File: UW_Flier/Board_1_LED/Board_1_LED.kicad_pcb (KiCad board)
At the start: 2 copper layers, 7.2 x 9.2 mm, 14 parts, among them J1 RESET, J2 SWDIO, J3 SWDCLK, J4 GND, J5 VDD, J6 LED_DRAIN, Q1 CSD13385F5, U1 EYSHSNZWZ_module_stub, Y1 Crystal

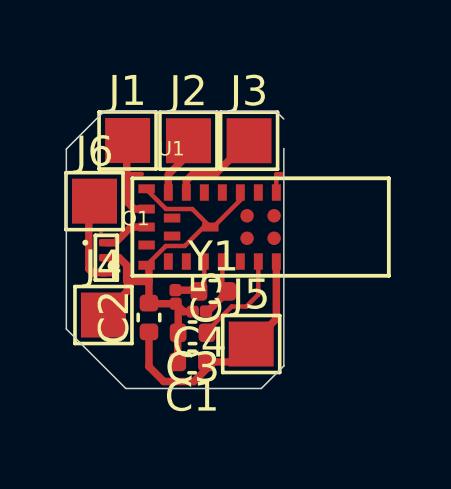
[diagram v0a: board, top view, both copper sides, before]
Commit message: added bmp384
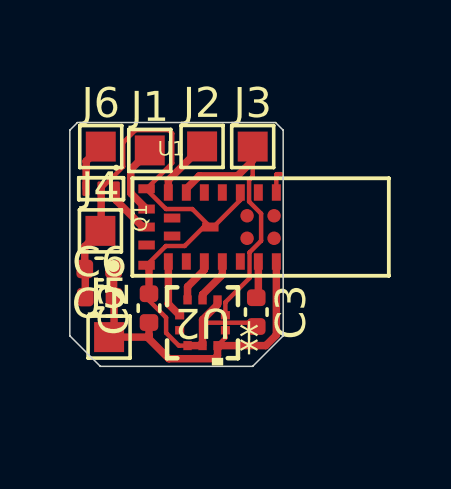
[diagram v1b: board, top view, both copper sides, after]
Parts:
- removed C4, C5: C, Capacitor_SMD:C_0201_0603Metric_Pad0.64x0.40mm_HandSolder
- removed Y1: Crystal, Capacitor_SMD:C_0402_1005Metric
- added C6: 100nF, Capacitor_SMD:C_0402_1005Metric, F.Cu at (103.6, 76.7)
- added U2: BMP384, footprints:LGA10_2.0X2.0X0.95_BOS, F.Cu at (107.0, 77.5)
- J1, J2, J3, J4, J5, J6: footprint CSD13385F5:TestPoint_Pad_1.5x1.5mm_2 -> TestPoint:TestPoint_Pad_1.0x1.0mm
- moved J5 4.74 mm to (103.9, 78.0)
- moved C1 4.38 mm to (103.6, 75.8)
- moved J4 2.81 mm to (103.6, 74.5)
- moved Q1 2.31 mm to (103.7, 73.1), turned to -90 degrees
- moved C3 2.23 mm to (108.8, 77.2), turned to -90 degrees
- moved J6 1.83 mm to (103.6, 71.7)
- moved J1 0.81 mm to (105.3, 71.8)
- moved J2 0.49 mm to (107.0, 71.7)
- moved C2 0.31 mm to (105.3, 77.1)
- moved J3 0.23 mm to (108.7, 71.7)
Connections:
- U1 pad 2: unconnected-(U1-P0.06-Pad2) -> Net-(U1-P0.06)
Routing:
- net Net-(J4-Pin_1): track 15.3 -> 24.3 mm
- net Net-(J3-Pin_1): track 3.04 -> 9.10 mm
- net Net-(J5-Pin_1): track 8.52 -> 12.3 mm
- net Net-(U1-DEC4): track 3.37 -> 1.23 mm
- net Net-(U1-P0.06): track 0.00 -> 1.95 mm
- net Net-(J6-Pin_1): track 2.97 -> 1.61 mm
- net Net-(J1-Pin_1): track 3.31 -> 2.43 mm
- net Net-(U1-P0.01/XL2): track 2.07 -> 1.55 mm
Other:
- board size 7.2 x 9.2 mm -> 7.1 x 8.1 mm
